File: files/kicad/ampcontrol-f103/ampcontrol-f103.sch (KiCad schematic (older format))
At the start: 62 parts, among them J1 Audio, J10 LCD_DATA, J11 LCD_CTRL, J12 Buttons, J13 Encoder, J14 I2C_Audio, J15 I2C_Tuner, J16 I2C_Ext, J2 MUTE_STBY, J3 UART, J4 USB, J5 UART2, J6 UART3, J7 RC, J8 SPI, J9 5V, Q1 BSS138, SW1 Reset, U1 MCP602, U2 STM32F103CBTx, U3 AMS1117-3.3, Y1 8MHz, Y2 32768

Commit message: PCB arrangement
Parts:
- removed J11: LCD_CTRL, Connector_PinHeader_2.54mm:PinHeader_1x06_P2.54mm_Vertical, symbol Connector_Generic:Conn_01x06
- removed J3: UART, Connector_PinHeader_2.54mm:PinHeader_1x04_P2.54mm_Vertical, symbol Connector_Generic:Conn_01x04
- removed J5: UART2, Connector_PinHeader_2.54mm:PinHeader_1x04_P2.54mm_Vertical, symbol Connector_Generic:Conn_01x04
- removed J6: UART3, Connector_PinHeader_2.54mm:PinHeader_1x04_P2.54mm_Vertical, symbol Connector_Generic:Conn_01x04
- added J12: LCD_CTRL, Connector_PinSocket_2.54mm:PinSocket_1x14_P2.54mm_Vertical, symbol Connector_Generic:Conn_01x14
- added J3: UART1, Connector_PinHeader_2.54mm:PinHeader_1x03_P2.54mm_Vertical, symbol Connector_Generic:Conn_01x03
- added J5: UART2, Connector_PinHeader_2.54mm:PinHeader_1x03_P2.54mm_Vertical, symbol Connector_Generic:Conn_01x03
- added J6: UART3, Connector_PinHeader_2.54mm:PinHeader_1x03_P2.54mm_Vertical, symbol Connector_Generic:Conn_01x03
- added R20: 4.7k, Resistor_SMD:R_0805_2012Metric, symbol Device:R
- J1: value Audio -> SP
- J13: renamed from J8; footprint Connector_PinHeader_2.54mm:PinHeader_1x04_P2.54mm_Vertical -> Connector_PinSocket_2.54mm:PinSocket_1x04_P2.54mm_Vertical
- J14: value I2C_Audio -> I2C
- J15: value I2C_Tuner -> I2C
- J16: value I2C_Ext -> I2C
- J8: renamed from J10; footprint Connector_PinHeader_2.54mm:PinHeader_1x08_P2.54mm_Vertical -> Connector_PinSocket_2.54mm:PinSocket_1x08_P2.54mm_Vertical
- renumbered C3 to C1, C1 to C2, C2 to C3, J12 to J10, J13 to J11, R20 to R21, R21 to R22, R22 to R23, RV2 to RV1, RV1 to RV2
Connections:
- net +3V3: now also J12.1 (Pin_1), R20.1
- net BCKL: now also J12.8 (Pin_8)
- net BTN_5: now also J11.1 (Pin_1); no longer J11.5 (Pin_5)
- net CS: now also J12.3 (Pin_3)
- net ENC_A: now also J11.3 (Pin_3); no longer J11.1 (Pin_1)
- net ENC_B: now also J11.5 (Pin_5); no longer J11.3 (Pin_3)
- net GNDD: now also J12.2 (Pin_2), J3.3 (Pin_3), J5.3 (Pin_3), J6.3 (Pin_3)
- net NRST: now also J12.4 (Pin_4)
- net RS: now also J12.5 (Pin_5)
- net RX2: now also J5.2 (Pin_2)
- net RX3: now also J6.2 (Pin_2)
- net SCK: now also J12.7 (Pin_7)
- net SD_CS: now also J13.1 (Pin_1); no longer J13.4 (Pin_4)
- net TX2: now also J5.1 (Pin_1)
- net TX3: now also J6.1 (Pin_1)
- net WR: now also J12.6 (Pin_6)
- net USB_M: now reaches J4.2 (Pin_2), R1.1
- net USB_P: now reaches J4.3 (Pin_3), R2.1
- net RX renamed RX1
- net RX1: now also J3.2 (Pin_2)
- net SD_CLK renamed SD_MOSI
- net SD_MOSI: now also U2.17 (PA7); no longer U2.15 (PA5)
- net SD_DIN renamed SD_MISO
- net SD_MISO: now also U2.16 (PA6); no longer U2.17 (PA7)
- removed net SD_DO: J13.1 (Pin_1), U2.16 (PA6)
- net TX renamed TX1
- net TX1: now also J3.1 (Pin_1)
- new net: J12.9 (Pin_9), R20.2
- new net SD_SCK: J13.4 (Pin_4), U2.15 (PA5)
- no-connect marks 0 -> 6
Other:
- moved on the sheet: BT1, C1, C14, J10, J11, J13, J8, R1, R12, R13, R14, R15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

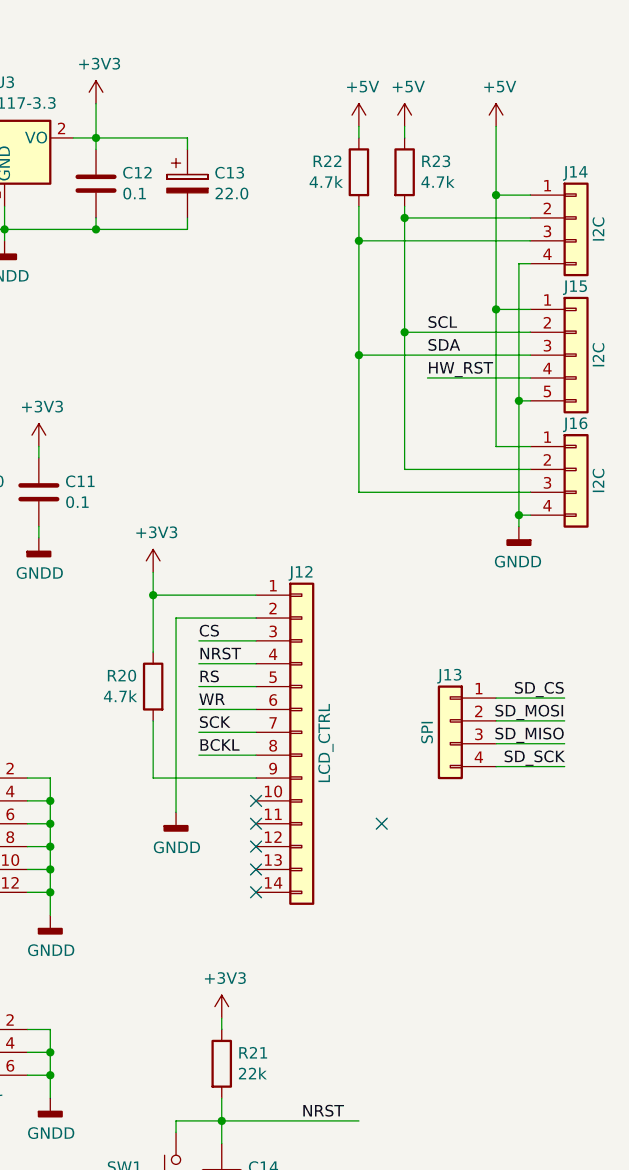
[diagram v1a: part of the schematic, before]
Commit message: Finish with ILI9341 SPI PCB
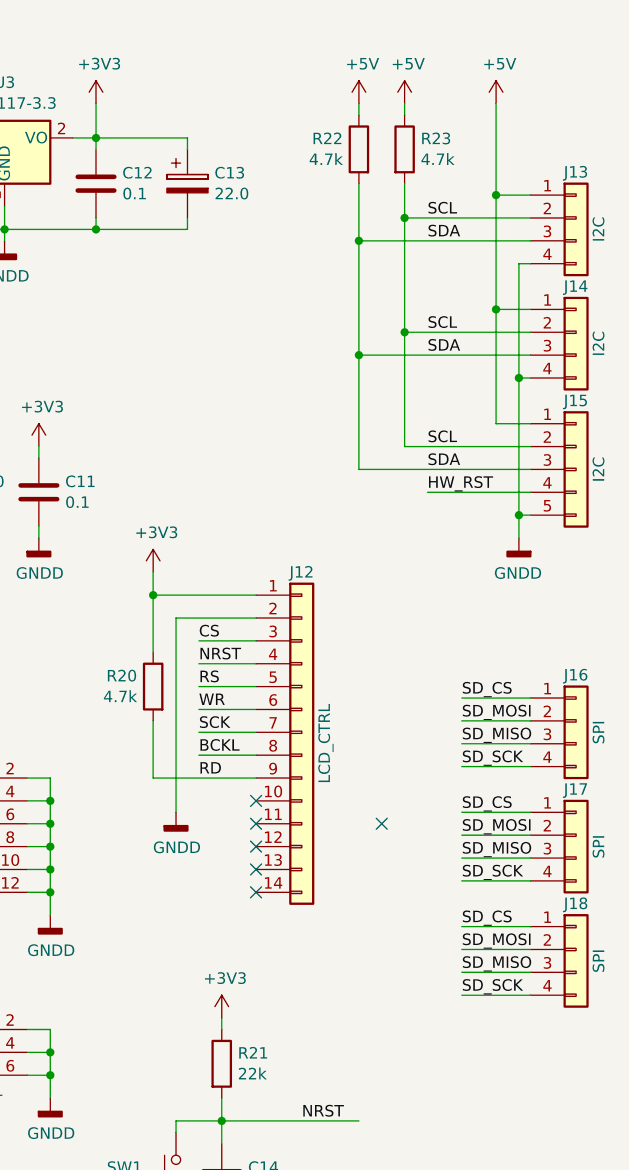
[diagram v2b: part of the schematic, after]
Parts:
- added J17, J18: SPI, Connector_PinSocket_2.54mm:PinSocket_1x04_P2.54mm_Vertical, symbol Connector_Generic:Conn_01x04
- renumbered J14 to J13, J16 to J14, J13 to J16
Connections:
- net SD_CS: now also J17.1 (Pin_1), J18.1 (Pin_1)
- net SD_MISO: now also J17.3 (Pin_3), J18.3 (Pin_3)
- net SD_MOSI: now also J17.2 (Pin_2), J18.2 (Pin_2)
- net SD_SCK: now also J17.4 (Pin_4), J18.4 (Pin_4)
- net RD: now reaches J12.9 (Pin_9), R20.2
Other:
- moved on the sheet: J14, J15, J16, R22, R23
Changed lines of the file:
@@
 	6250 6200 6500 6200
 Wire Wire Line
-	10400 3800 10700 3800
-Wire Wire Line
-	10400 3900 10700 3900
-Wire Wire Line
-	10400 3700 10700 3700
-Wire Wire Line
-	10400 3600 10700 3600
+	10550 3800 10250 3800
+Wire Wire Line
+	10550 3900 10250 3900
+Wire Wire Line
+	10550 3700 10250 3700
+Wire Wire Line
+	10550 3600 10250 3600
 Text Label 6250 5500 0    50   ~ 0
 DB0
@@
 Text Label 6250 6200 0    50   ~ 0
 DB7
-Text Label 10700 3800 2    50   ~ 0
+Text Label 10250 3800 0    50   ~ 0
 SD_MISO
-Text Label 10700 3900 2    50   ~ 0
+Text Label 10250 3900 0    50   ~ 0
 SD_SCK
-Text Label 10700 3700 2    50   ~ 0
+Text Label 10250 3700 0    50   ~ 0
 SD_MOSI
-Text Label 10700 3600 2    50   ~ 0
+Text Label 10250 3600 0    50   ~ 0
 SD_CS
 $Comp
@@
 L power:+5V #PWR041
 U 1 1 5C166122
-P 9800 1100
-F 0 "#PWR041" H 9800 950 50  0001 C CNN
-F 1 "+5V" H 9815 1273 50  0000 C CNN
-F 2 "" H 9800 1100 50  0001 C CNN
-F 3 "" H 9800 1100 50  0001 C CNN
-	1    9800 1100
+P 9800 1000
+F 0 "#PWR041" H 9800 850 50  0001 C CNN
+F 1 "+5V" H 9815 1173 50  0000 C CNN
+F 2 "" H 9800 1000 50  0001 C CNN
+F 3 "" H 9800 1000 50  0001 C CNN
+	1    9800 1000
 	1    0    0    -1
 $EndComp
@@
 L Device:R R22
 U 1 1 5C166181
-P 9800 1300
-F 0 "R22" H 9870 1346 50  0000 L CNN
-F 1 "4.7k" H 9870 1255 50  0000 L CNN
-F 2 "Resistor_SMD:R_0805_2012Metric" V 9730 1300 50  0001 C CNN
-F 3 "~" H 9800 1300 50  0001 C CNN
-	1    9800 1300
+P 9800 1200
+F 0 "R22" H 9870 1246 50  0000 L CNN
+F 1 "4.7k" H 9870 1155 50  0000 L CNN
+F 2 "Resistor_SMD:R_0805_2012Metric" V 9730 1200 50  0001 C CNN
+F 3 "~" H 9800 1200 50  0001 C CNN
+	1    9800 1200
 	-1   0    0    -1
 $EndComp
@@
 L power:+5V #PWR042
 U 1 1 5C16F716
-P 10000 1100
-F 0 "#PWR042" H 10000 950 50  0001 C CNN
-F 1 "+5V" H 10015 1273 50  0000 C CNN
-F 2 "" H 10000 1100 50  0001 C CNN
-F 3 "" H 10000 1100 50  0001 C CNN
-	1    10000 1100
+P 10000 1000
+F 0 "#PWR042" H 10000 850 50  0001 C CNN
+F 1 "+5V" H 10015 1173 50  0000 C CNN
+F 2 "" H 10000 1000 50  0001 C CNN
+F 3 "" H 10000 1000 50  0001 C CNN
+	1    10000 1000
 	1    0    0    -1
 $EndComp
@@
 L Device:R R23
 U 1 1 5C16F733
-P 10000 1300
-F 0 "R23" H 10070 1346 50  0000 L CNN
-F 1 "4.7k" H 10070 1255 50  0000 L CNN
-F 2 "Resistor_SMD:R_0805_2012Metric" V 9930 1300 50  0001 C CNN
-F 3 "~" H 10000 1300 50  0001 C CNN
-	1    10000 1300
-	1    0    0    -1
-$EndComp
-Wire Wire Line
-	9800 1150 9800 1100
-Wire Wire Line
-	10000 1100 10000 1150
+P 10000 1200
+F 0 "R23" H 10070 1246 50  0000 L CNN
+F 1 "4.7k" H 10070 1155 50  0000 L CNN
+F 2 "Resistor_SMD:R_0805_2012Metric" V 9930 1200 50  0001 C CNN
+F 3 "~" H 10000 1200 50  0001 C CNN
+	1    10000 1200
+	1    0    0    -1
+$EndComp
+Wire Wire Line
+	9800 1050 9800 1000
+Wire Wire Line
+	10000 1000 10000 1050
 Wire Wire Line
 	4050 5950 3650 5950
@@
 L Connector_Generic:Conn_01x05 J15
 U 1 1 5D48492A
-P 10750 2100
-F 0 "J15" H 10750 2400 50  0000 C CNN
-F 1 "I2C" V 10850 2100 50  0000 C CNN
-F 2 "Connector_PinHeader_2.54mm:PinHeader_1x05_P2.54mm_Vertical" H 10750 2100 50  0001 C CNN
-F 3 "~" H 10750 2100 50  0001 C CNN
-	1    10750 2100
+P 10750 2600
+F 0 "J15" H 10750 2900 50  0000 C CNN
+F 1 "I2C" V 10850 2600 50  0000 C CNN
+F 2 "Connector_PinHeader_2.54mm:PinHeader_1x05_P2.54mm_Vertical" H 10750 2600 50  0001 C CNN
+F 3 "~" H 10750 2600 50  0001 C CNN
+	1    10750 2600
 	1    0    0    -1
 $EndComp
@@
 Wire Wire Line
 	10400 1900 10550 1900
-Text Label 10100 2200 0    50   ~ 0
+Text Label 10100 2700 0    50   ~ 0
 HW_RST
-Wire Wire Line
-	10550 2300 10500 2300
 Wire Wire Line
 	1750 6800 1750 6950
@@
 SCK
 $Comp
-L Connector_Generic:Conn_01x04 J13
+L Connector_Generic:Conn_01x04 J16
 U 1 1 5CE30DC8
-P 10200 3700
-F 0 "J13" H 10200 3900 50  0000 C CNN
-F 1 "SPI" V 10300 3650 50  0000 C CNN
-F 2 "Connector_PinSocket_2.54mm:PinSocket_1x04_P2.54mm_Vertical" H 10200 3700 50  0001 C CNN
-F 3 "~" H 10200 3700 50  0001 C CNN
-	1    10200 3700
-	-1   0    0    -1
+P 10750 3700
+F 0 "J16" H 10750 3900 50  0000 C CNN
+F 1 "SPI" V 10850 3650 50  0000 C CNN
+F 2 "Connector_PinSocket_2.54mm:PinSocket_1x04_P2.54mm_Vertical" H 10750 3700 50  0001 C CNN
+F 3 "~" H 10750 3700 50  0001 C CNN
+	1    10750 3700
+	1    0    0    -1
 $EndComp
 Wire Wire Line
@@
 L power:+5V #PWR043
 U 1 1 5D3E2AA0
-P 10400 1100
-F 0 "#PWR043" H 10400 950 50  0001 C CNN
-F 1 "+5V" H 10415 1273 50  0000 C CNN
-F 2 "" H 10400 1100 50  0001 C CNN
-F 3 "" H 10400 1100 50  0001 C CNN
-	1    10400 1100
+P 10400 1000
+F 0 "#PWR043" H 10400 850 50  0001 C CNN
+F 1 "+5V" H 10415 1173 50  0000 C CNN
+F 2 "" H 10400 1000 50  0001 C CNN
+F 3 "" H 10400 1000 50  0001 C CNN
+	1    10400 1000
 	1    0    0    -1
 $EndComp
@@
 L power:GNDD #PWR044
 U 1 1 5D3191F5
-P 10500 2850
-F 0 "#PWR044" H 10500 2600 50  0001 C CNN
-F 1 "GNDD" H 10504 2695 50  0000 C CNN
-F 2 "" H 10500 2850 50  0001 C CNN
-F 3 "" H 10500 2850 50  0001 C CNN
-	1    10500 2850
+P 10500 2900
+F 0 "#PWR044" H 10500 2650 50  0001 C CNN
+F 1 "GNDD" H 10504 2745 50  0000 C CNN
+F 2 "" H 10500 2900 50  0001 C CNN
+F 3 "" H 10500 2900 50  0001 C CNN
+	1    10500 2900
 	-1   0    0    -1
 $EndComp
 Wire Wire Line
-	9800 1450 9800 1600
-Wire Wire Line
-	10000 1450 10000 1500
-Wire Wire Line
-	10400 1100 10400 1400
-Wire Wire Line
-	10100 2200 10550 2200
-Wire Wire Line
-	10500 2300 10500 2800
+	9800 1350 9800 1600
+Wire Wire Line
+	10000 1350 10000 1500
+Wire Wire Line
+	10400 1000 10400 1400
+Wire Wire Line
+	10100 2700 10550 2700
 $Comp
 L Connector_Generic:Conn_01x14 J12
@@
 	10550 1700 10500 1700
 Wire Wire Line
-	10500 1700 10500 2300
-Connection ~ 10500 2300
-Wire Wire Line
-	10550 2800 10500 2800
-Connection ~ 10500 2800
-Wire Wire Line
-	10500 2800 10500 2850
-Wire Wire Line
-	10550 2500 10400 2500
-Wire Wire Line
-	10400 2500 10400 1900
+	10550 2400 10400 2400
+Wire Wire Line
+	10400 2400 10400 1900
 Connection ~ 10400 1900
 Wire Wire Line
@@
 	9800 1600 9800 2100
 Wire Wire Line
-	10550 2600 10000 2600
-Wire Wire Line
-	10000 2600 10000 2000
+	10550 2500 10000 2500
+Wire Wire Line
+	10000 2500 10000 2000
 Connection ~ 10000 2000
 Wire Wire Line
-	10550 2700 9800 2700
-Wire Wire Line
-	9800 2700 9800 2100
+	10550 2600 9800 2600
+Wire Wire Line
+	9800 2600 9800 2100
 Connection ~ 9800 2100
 $Comp
-L Connector_Generic:Conn_01x04 J14
+L Connector_Generic:Conn_01x04 J13
 U 1 1 5C867CD5
 P 10750 1500
-F 0 "J14" H 10750 1700 50  0000 C CNN
+F 0 "J13" H 10750 1700 50  0000 C CNN
 F 1 "I2C" V 10850 1450 50  0000 C CNN
 F 2 "Connector_PinHeader_2.54mm:PinHeader_1x04_P2.54mm_Vertical" H 10750 1500 50  0001 C CNN
@@
 $EndComp
 $Comp
-L Connector_Generic:Conn_01x04 J16
+L Connector_Generic:Conn_01x04 J14
 U 1 1 5C87E514
-P 10750 2600
-F 0 "J16" H 10750 2800 50  0000 C CNN
-F 1 "I2C" V 10850 2550 50  0000 C CNN
-F 2 "Connector_PinHeader_2.54mm:PinHeader_1x04_P2.54mm_Vertical" H 10750 2600 50  0001 C CNN
-F 3 "~" H 10750 2600 50  0001 C CNN
-	1    10750 2600
+P 10750 2000
+F 0 "J14" H 10750 2200 50  0000 C CNN
+F 1 "I2C" V 10850 1950 50  0000 C CNN
+F 2 "Connector_PinHeader_2.54mm:PinHeader_1x04_P2.54mm_Vertical" H 10750 2000 50  0001 C CNN
+F 3 "~" H 10750 2000 50  0001 C CNN
+	1    10750 2000
 	1    0    0    -1
 $EndComp
@@
 Wire Wire Line
 	2700 5250 2700 5350
+Wire Wire Line
+	10500 1700 10500 2200
+Wire Wire Line
+	10550 2200 10500 2200
+Connection ~ 10500 2200
+Wire Wire Line
+	10500 2200 10500 2800
+Wire Wire Line
+	10550 2800 10500 2800
+Connection ~ 10500 2800
+Wire Wire Line
+	10500 2800 10500 2900
+Text Label 10100 2500 0    50   ~ 0
+SCL
+Text Label 10100 2600 0    50   ~ 0
+SDA
+Text Label 10100 1500 0    50   ~ 0
+SCL
+Text Label 10100 1600 0    50   ~ 0
+SDA
+Wire Wire Line
+	10550 4300 10250 4300
+Wire Wire Line
+	10550 4400 10250 4400
+Wire Wire Line
+	10550 4200 10250 4200
+Wire Wire Line
+	10550 4100 10250 4100
+Text Label 10250 4300 0    50   ~ 0
+SD_MISO
+Text Label 10250 4400 0    50   ~ 0
+SD_SCK
+Text Label 10250 4200 0    50   ~ 0
+SD_MOSI
+Text Label 10250 4100 0    50   ~ 0
+SD_CS
+$Comp
+L Connector_Generic:Conn_01x04 J17
+U 1 1 5C867944
+P 10750 4200
+F 0 "J17" H 10750 4400 50  0000 C CNN
+F 1 "SPI" V 10850 4150 50  0000 C CNN
+F 2 "Connector_PinSocket_2.54mm:PinSocket_1x04_P2.54mm_Vertical" H 10750 4200 50  0001 C CNN
+F 3 "~" H 10750 4200 50  0001 C CNN
+	1    10750 4200
+	1    0    0    -1
+$EndComp
+Wire Wire Line
+	10550 4800 10250 4800
+Wire Wire Line
+	10550 4900 10250 4900
+Wire Wire Line
+	10550 4700 10250 4700
+Wire Wire Line
+	10550 4600 10250 4600
+Text Label 10250 4800 0    50   ~ 0
+SD_MISO
+Text Label 10250 4900 0    50   ~ 0
+SD_SCK
+Text Label 10250 4700 0    50   ~ 0
+SD_MOSI
+Text Label 10250 4600 0    50   ~ 0
+SD_CS
+$Comp
+L Connector_Generic:Conn_01x04 J18
+U 1 1 5C897991
+P 10750 4700
+F 0 "J18" H 10750 4900 50  0000 C CNN
+F 1 "SPI" V 10850 4650 50  0000 C CNN
+F 2 "Connector_PinSocket_2.54mm:PinSocket_1x04_P2.54mm_Vertical" H 10750 4700 50  0001 C CNN
+F 3 "~" H 10750 4700 50  0001 C CNN
+	1    10750 4700
+	1    0    0    -1
+$EndComp
+Text Label 9100 3950 0    50   ~ 0
+RD
 $EndSCHEMATC
